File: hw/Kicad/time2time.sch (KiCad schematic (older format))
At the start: 0 parts

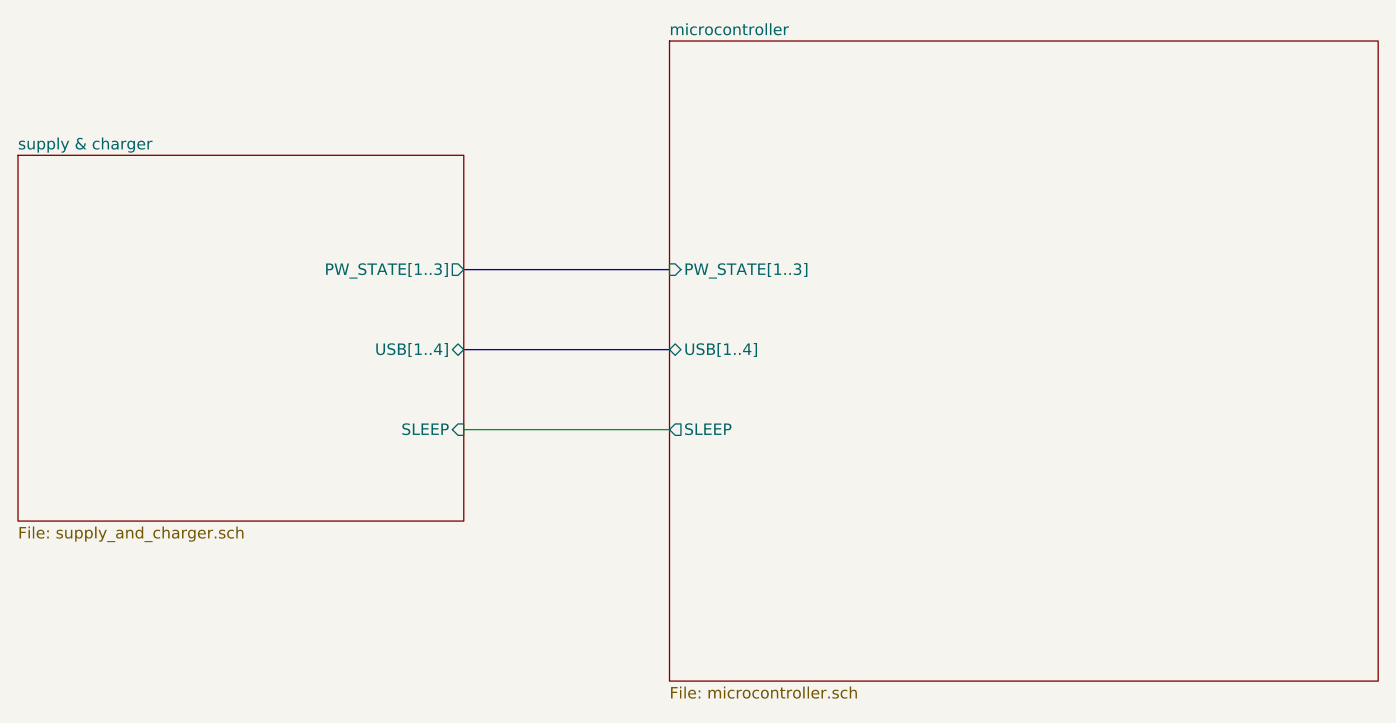
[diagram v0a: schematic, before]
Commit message: V1.1 version. UART fixed and some signals renamed
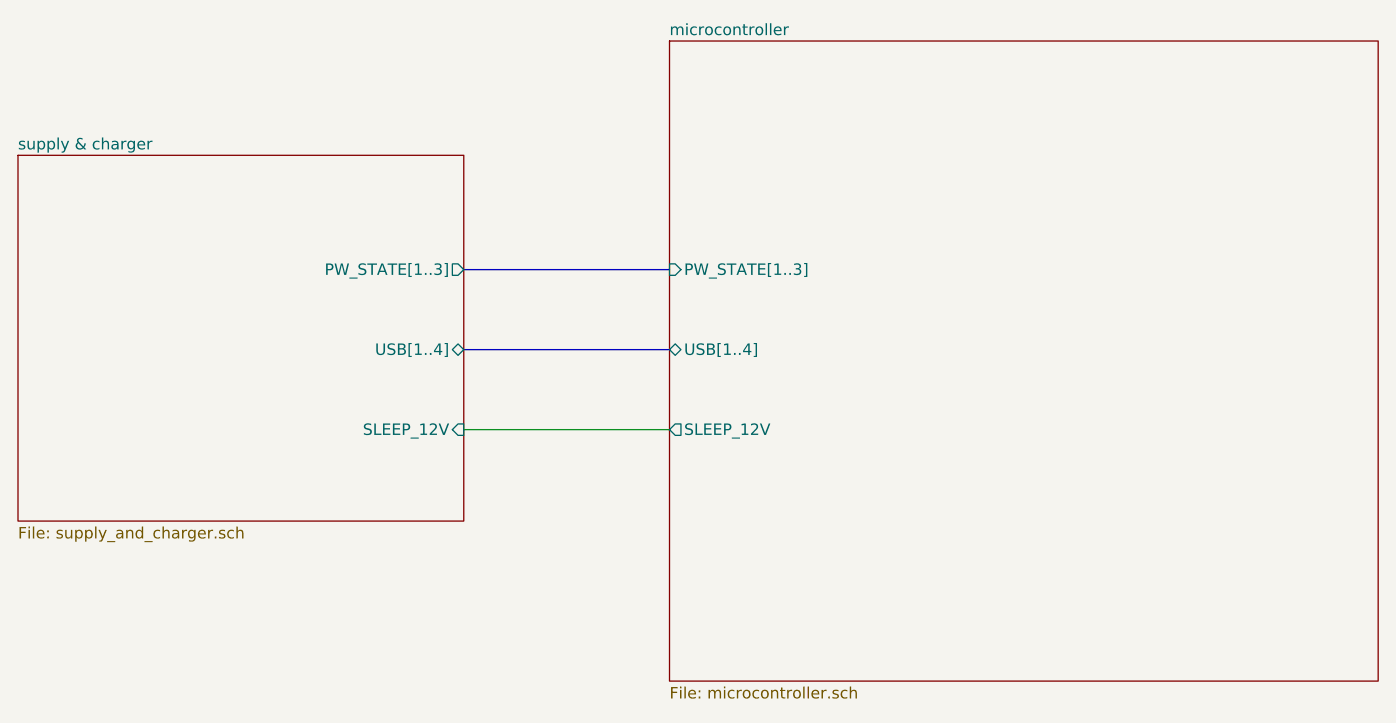
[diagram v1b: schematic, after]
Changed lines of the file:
@@
 Sheet 1 3
 Title "time2time project"
-Date "2019-09-09"
-Rev "V1.0"
+Date "2019-10-29"
+Rev "V1.1"
 Comp "Puma Pride Robotics Team"
 Comment1 "Designed by Rubén Espino San José"
@@
 F2 "USB[1..4]" B R 4600 3650 50
 F3 "PW_STATE[1..3]" O R 4600 3300 50
-F4 "SLEEP" I R 4600 4000 50
+F4 "SLEEP_12V" I R 4600 4000 50
 $EndSheet
 $Sheet
@@
 F2 "USB[1..4]" B L 5500 3650 50
 F3 "PW_STATE[1..3]" I L 5500 3300 50
-F4 "SLEEP" O L 5500 4000 50
+F4 "SLEEP_12V" O L 5500 4000 50
 $EndSheet
 Wire Bus Line
